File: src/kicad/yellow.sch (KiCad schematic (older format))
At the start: 0 parts

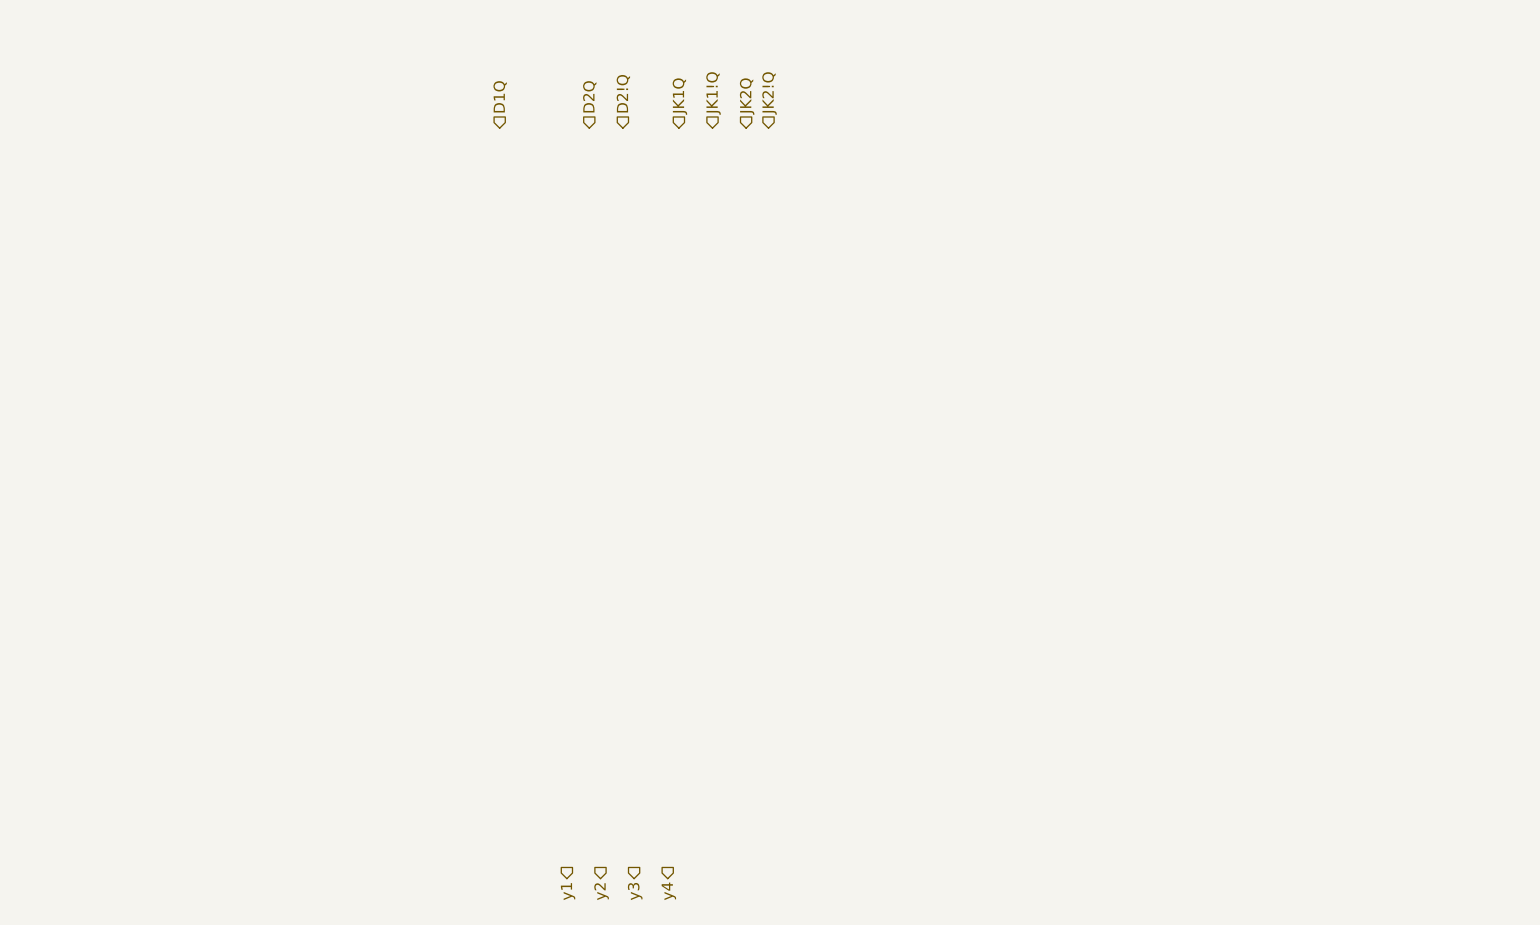
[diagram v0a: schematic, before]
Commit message: finished sub-schemes for LEDs
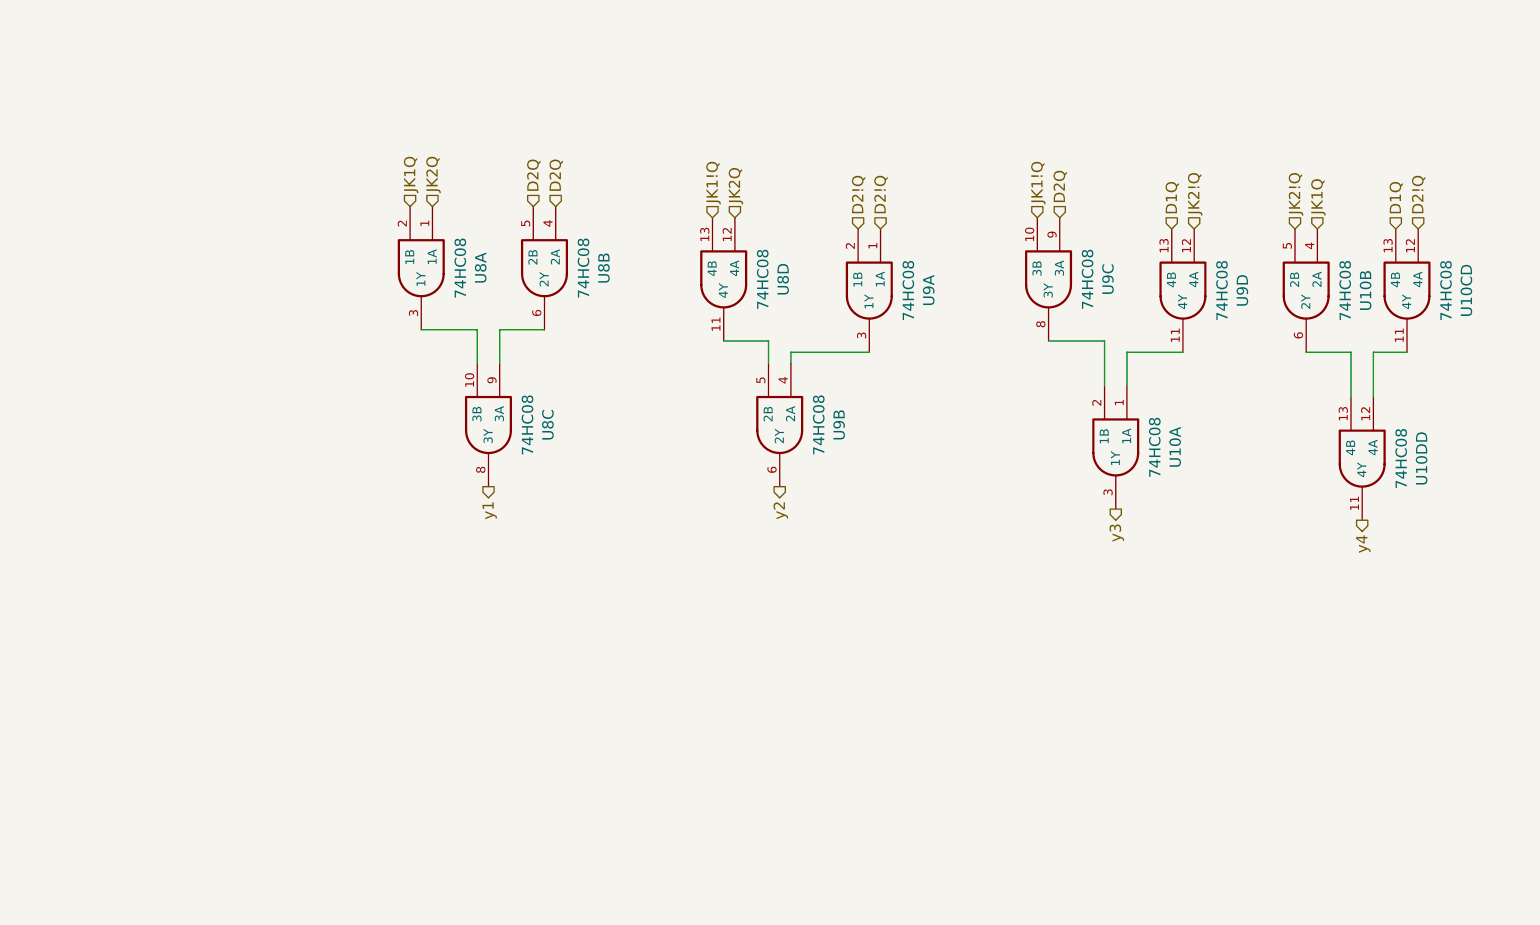
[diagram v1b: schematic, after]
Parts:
- added U10, U10C, U10D, U8, U9: 74HC08, Housings_SOIC:SOIC-14_3.9x8.7mm_Pitch1.27mm, symbol PB170:74HC08
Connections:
- net D1Q: now also U10C.13 (4B), U9.13 (4B)
- net D2!Q: now also U10C.12 (4A), U9.1 (1A), U9.2 (1B)
- net D2Q: now also U8.4 (2A), U8.5 (2B), U9.9 (3A)
- net JK1!Q: now also U8.13 (4B), U9.10 (3B)
- net JK1Q: now also U10.4 (2A), U8.2 (1B)
- net JK2!Q: now also U10.5 (2B), U9.12 (4A)
- net JK2Q: now also U8.1 (1A), U8.12 (4A)
- net y1: now also U8.8 (3Y)
- net y2: now also U9.6 (2Y)
- net y3: now also U10.3 (1Y)
- net y4: now also U10D.11 (4Y)
- new net: U8.10 (3B), U8.3 (1Y)
- new net: U8.6 (2Y), U8.9 (3A)
- new net: U8.11 (4Y), U9.5 (2B)
- new net: U9.3 (1Y), U9.4 (2A)
- new net: U10.2 (1B), U9.8 (3Y)
- new net: U10.1 (1A), U9.11 (4Y)
- new net: U10.6 (2Y), U10D.13 (4B)
- new net: U10C.11 (4Y), U10D.12 (4A)

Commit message: added OR gates
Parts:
- renumbered U10C to U10, U10D to U10
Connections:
- net D1Q: now also U10.10 (3B); no longer U10.13 (4B)
- net D2!Q: now also U10.9 (3A); no longer U10.12 (4A)
- net at U10.12 (4A): now also U10.8 (3Y); no longer U10.11 (4Y)
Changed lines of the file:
@@
 $Comp
 L PB170:74HC08 U?
-U 4 1 5FFFEFCB
+U 3 1 5FFFEFCB
 P 6850 2950
 AR Path="/5FFFEFCB" Ref="U?"  Part="2"
 AR Path="/6006FC3B/5FFFEFCB" Ref="U?"  Part="4"
 AR Path="/6004480C/5FFFEFCB" Ref="U?"  Part="4"
-AR Path="/60019DBB/5FFFEFCB" Ref="U10C"  Part="4"
-F 0 "U10C" H 6875 3217 50  0000 C CNN
+AR Path="/60019DBB/5FFFEFCB" Ref="U10"  Part="3"
+F 0 "U10" H 6875 3217 50  0000 C CNN
 F 1 "74HC08" H 6875 3126 50  0000 C CNN
 F 2 "Housings_SOIC:SOIC-14_3.9x8.7mm_Pitch1.27mm" H 6850 2950 50  0001 C CNN
 F 3 "https://datasheet.lcsc.com/szlcsc/Nexperia-74HC08D-653_C5593.pdf" H 6850 2950 50  0001 C CNN
 F 4 "C5593" H 6850 2950 50  0001 C CNN "LCSC"
-	4    6850 2950
+	3    6850 2950
 	0    1    1    0
 $EndComp
@@
 AR Path="/6006FC3B/5FFFF667" Ref="U?"  Part="4"
 AR Path="/6004480C/5FFFF667" Ref="U?"  Part="4"
-AR Path="/60019DBB/5FFFF667" Ref="U10D"  Part="4"
-F 0 "U10D" H 6675 3967 50  0000 C CNN
+AR Path="/60019DBB/5FFFF667" Ref="U10"  Part="4"
+F 0 "U10" H 6675 3967 50  0000 C CNN
 F 1 "74HC08" H 6675 3876 50  0000 C CNN
 F 2 "Housings_SOIC:SOIC-14_3.9x8.7mm_Pitch1.27mm" H 6650 3700 50  0001 C CNN

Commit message: fixed annotaion
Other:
- moved on the sheet: U10C
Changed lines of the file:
@@
 $Descr A4 11693 8268
 encoding utf-8
-Sheet 3 6
+Sheet 2 5
 Title ""
 Date ""
@@
 AR Path="/6004480C/5FFFB610" Ref="U?"  Part="4"
 AR Path="/60019DBB/5FFFB610" Ref="U8"  Part="1"
-F 0 "U8" H 2475 3117 50  0000 C CNN
-F 1 "74HC08" H 2475 3026 50  0000 C CNN
+F 0 "U8" V 2475 3117 50  0000 C CNN
+F 1 "74HC08" V 2400 3100 50  0000 C CNN
 F 2 "Housings_SOIC:SOIC-14_3.9x8.7mm_Pitch1.27mm" H 2450 2850 50  0001 C CNN
 F 3 "https://datasheet.lcsc.com/szlcsc/Nexperia-74HC08D-653_C5593.pdf" H 2450 2850 50  0001 C CNN
@@
 AR Path="/6004480C/5FFFBBCA" Ref="U?"  Part="4"
 AR Path="/60019DBB/5FFFBBCA" Ref="U8"  Part="2"
-F 0 "U8" H 3025 3117 50  0000 C CNN
-F 1 "74HC08" H 3025 3026 50  0000 C CNN
+F 0 "U8" V 3025 3117 50  0000 C CNN
+F 1 "74HC08" V 2950 3100 50  0000 C CNN
 F 2 "Housings_SOIC:SOIC-14_3.9x8.7mm_Pitch1.27mm" H 3000 2850 50  0001 C CNN
 F 3 "https://datasheet.lcsc.com/szlcsc/Nexperia-74HC08D-653_C5593.pdf" H 3000 2850 50  0001 C CNN
@@
 AR Path="/6004480C/5FFFC170" Ref="U?"  Part="4"
 AR Path="/60019DBB/5FFFC170" Ref="U8"  Part="3"
-F 0 "U8" H 2775 3817 50  0000 C CNN
-F 1 "74HC08" H 2775 3726 50  0000 C CNN
+F 0 "U8" V 2775 3817 50  0000 C CNN
+F 1 "74HC08" V 2700 3800 50  0000 C CNN
 F 2 "Housings_SOIC:SOIC-14_3.9x8.7mm_Pitch1.27mm" H 2750 3550 50  0001 C CNN
 F 3 "https://datasheet.lcsc.com/szlcsc/Nexperia-74HC08D-653_C5593.pdf" H 2750 3550 50  0001 C CNN
@@
 AR Path="/6004480C/5FFFC974" Ref="U?"  Part="4"
 AR Path="/60019DBB/5FFFC974" Ref="U8"  Part="4"
-F 0 "U8" H 3825 3167 50  0000 C CNN
-F 1 "74HC08" H 3825 3076 50  0000 C CNN
+F 0 "U8" V 3825 3167 50  0000 C CNN
+F 1 "74HC08" V 3750 3150 50  0000 C CNN
 F 2 "Housings_SOIC:SOIC-14_3.9x8.7mm_Pitch1.27mm" H 3800 2900 50  0001 C CNN
 F 3 "https://datasheet.lcsc.com/szlcsc/Nexperia-74HC08D-653_C5593.pdf" H 3800 2900 50  0001 C CNN
@@
 AR Path="/6004480C/5FFFCE4C" Ref="U?"  Part="4"
 AR Path="/60019DBB/5FFFCE4C" Ref="U9"  Part="1"
-F 0 "U9" H 4475 3217 50  0000 C CNN
-F 1 "74HC08" H 4475 3126 50  0000 C CNN
+F 0 "U9" V 4475 3217 50  0000 C CNN
+F 1 "74HC08" V 4400 3200 50  0000 C CNN
 F 2 "Housings_SOIC:SOIC-14_3.9x8.7mm_Pitch1.27mm" H 4450 2950 50  0001 C CNN
 F 3 "https://datasheet.lcsc.com/szlcsc/Nexperia-74HC08D-653_C5593.pdf" H 4450 2950 50  0001 C CNN
@@
 AR Path="/6004480C/5FFFD1FC" Ref="U?"  Part="4"
 AR Path="/60019DBB/5FFFD1FC" Ref="U9"  Part="2"
-F 0 "U9" H 4075 3817 50  0000 C CNN
-F 1 "74HC08" H 4075 3726 50  0000 C CNN
+F 0 "U9" V 4075 3817 50  0000 C CNN
+F 1 "74HC08" V 4000 3800 50  0000 C CNN
 F 2 "Housings_SOIC:SOIC-14_3.9x8.7mm_Pitch1.27mm" H 4050 3550 50  0001 C CNN
 F 3 "https://datasheet.lcsc.com/szlcsc/Nexperia-74HC08D-653_C5593.pdf" H 4050 3550 50  0001 C CNN
@@
 AR Path="/6004480C/5FFFD73E" Ref="U?"  Part="4"
 AR Path="/60019DBB/5FFFD73E" Ref="U9"  Part="3"
-F 0 "U9" H 5275 3167 50  0000 C CNN
-F 1 "74HC08" H 5275 3076 50  0000 C CNN
+F 0 "U9" V 5275 3167 50  0000 C CNN
+F 1 "74HC08" V 5200 3150 50  0000 C CNN
 F 2 "Housings_SOIC:SOIC-14_3.9x8.7mm_Pitch1.27mm" H 5250 2900 50  0001 C CNN
 F 3 "https://datasheet.lcsc.com/szlcsc/Nexperia-74HC08D-653_C5593.pdf" H 5250 2900 50  0001 C CNN
@@
 AR Path="/6004480C/5FFFDB52" Ref="U?"  Part="4"
 AR Path="/60019DBB/5FFFDB52" Ref="U9"  Part="4"
-F 0 "U9" H 5875 3217 50  0000 C CNN
-F 1 "74HC08" H 5875 3126 50  0000 C CNN
+F 0 "U9" V 5875 3217 50  0000 C CNN
+F 1 "74HC08" V 5800 3200 50  0000 C CNN
 F 2 "Housings_SOIC:SOIC-14_3.9x8.7mm_Pitch1.27mm" H 5850 2950 50  0001 C CNN
 F 3 "https://datasheet.lcsc.com/szlcsc/Nexperia-74HC08D-653_C5593.pdf" H 5850 2950 50  0001 C CNN
@@
 AR Path="/6004480C/5FFFDDDA" Ref="U?"  Part="4"
 AR Path="/60019DBB/5FFFDDDA" Ref="U10"  Part="1"
-F 0 "U10" H 5575 3917 50  0000 C CNN
-F 1 "74HC08" H 5575 3826 50  0000 C CNN
+F 0 "U10" V 5575 3917 50  0000 C CNN
+F 1 "74HC08" V 5500 3900 50  0000 C CNN
 F 2 "Housings_SOIC:SOIC-14_3.9x8.7mm_Pitch1.27mm" H 5550 3650 50  0001 C CNN
 F 3 "https://datasheet.lcsc.com/szlcsc/Nexperia-74HC08D-653_C5593.pdf" H 5550 3650 50  0001 C CNN
@@
 AR Path="/6004480C/5FFFE731" Ref="U?"  Part="4"
 AR Path="/60019DBB/5FFFE731" Ref="U10"  Part="2"
-F 0 "U10" H 6425 3217 50  0000 C CNN
-F 1 "74HC08" H 6425 3126 50  0000 C CNN
+F 0 "U10" V 6450 3200 50  0000 C CNN
+F 1 "74HC08" V 6350 3200 50  0000 C CNN
 F 2 "Housings_SOIC:SOIC-14_3.9x8.7mm_Pitch1.27mm" H 6400 2950 50  0001 C CNN
 F 3 "https://datasheet.lcsc.com/szlcsc/Nexperia-74HC08D-653_C5593.pdf" H 6400 2950 50  0001 C CNN
@@
 L PB170:74HC08 U?
 U 3 1 5FFFEFCB
-P 6850 2950
+P 6950 2950
 AR Path="/5FFFEFCB" Ref="U?"  Part="2"
 AR Path="/6006FC3B/5FFFEFCB" Ref="U?"  Part="4"
 AR Path="/6004480C/5FFFEFCB" Ref="U?"  Part="4"
 AR Path="/60019DBB/5FFFEFCB" Ref="U10"  Part="3"
-F 0 "U10" H 6875 3217 50  0000 C CNN
-F 1 "74HC08" H 6875 3126 50  0000 C CNN
-F 2 "Housings_SOIC:SOIC-14_3.9x8.7mm_Pitch1.27mm" H 6850 2950 50  0001 C CNN
-F 3 "https://datasheet.lcsc.com/szlcsc/Nexperia-74HC08D-653_C5593.pdf" H 6850 2950 50  0001 C CNN
-F 4 "C5593" H 6850 2950 50  0001 C CNN "LCSC"
-	3    6850 2950
+F 0 "U10" V 6975 3217 50  0000 C CNN
+F 1 "74HC08" V 6900 3200 50  0000 C CNN
+F 2 "Housings_SOIC:SOIC-14_3.9x8.7mm_Pitch1.27mm" H 6950 2950 50  0001 C CNN
+F 3 "https://datasheet.lcsc.com/szlcsc/Nexperia-74HC08D-653_C5593.pdf" H 6950 2950 50  0001 C CNN
+F 4 "C5593" H 6950 2950 50  0001 C CNN "LCSC"
+	3    6950 2950
 	0    1    1    0
 $EndComp
@@
 AR Path="/6004480C/5FFFF667" Ref="U?"  Part="4"
 AR Path="/60019DBB/5FFFF667" Ref="U10"  Part="4"
-F 0 "U10" H 6675 3967 50  0000 C CNN
-F 1 "74HC08" H 6675 3876 50  0000 C CNN
+F 0 "U10" V 6675 3967 50  0000 C CNN
+F 1 "74HC08" V 6600 3950 50  0000 C CNN
 F 2 "Housings_SOIC:SOIC-14_3.9x8.7mm_Pitch1.27mm" H 6650 3700 50  0001 C CNN
 F 3 "https://datasheet.lcsc.com/szlcsc/Nexperia-74HC08D-653_C5593.pdf" H 6650 3700 50  0001 C CNN
@@
 	6600 3250 6600 3450
 Wire Wire Line
-	6850 3250 6700 3250
+	6950 3250 6700 3250
 Wire Wire Line
 	6700 3250 6700 3450
@@
 Text HLabel 6450 2700 1    50   Input ~ 0
 JK1Q
-Text HLabel 6800 2700 1    50   Input ~ 0
+Text HLabel 6900 2700 1    50   Input ~ 0
 D1Q
-Text HLabel 6900 2700 1    50   Input ~ 0
+Text HLabel 7000 2700 1    50   Input ~ 0
 D2!Q
 $EndSCHEMATC
